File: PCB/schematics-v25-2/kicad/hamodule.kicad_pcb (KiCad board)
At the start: 4 copper layers, 129.6 x 83.3 mm, 200 parts, among them J1 GND|5V, J10 Tx|Rx, J11 Sda|Scl, J12 3|9, J13 13|12, J14 3.3v|GND|7|15, J15 2604-1104, J16 2604-1104, J17 TestPoint, J19 TestPoint, J2 2604-1102, J3 USB_C_Receptacle_USB2.0, J4 GND|3.3V, J5 Conn_01x02_Pin, J6 2604-1104, J7 2604-1104, J8 5v|GND|Do, J9 Screen, K1 AQG22205, K2 AQG22205, K3 AQG22205, K4 AQG22205, K5 AQG22205, K6 AQG22205, K7 AQG22205, K8 AQG22205, SW1 USB | PS, SW2 Reset, SW3 Boot, U1 LD1117AV33, U10 SN74LV1T34DBV, U11 ULN2803A, U12 TCAL6416, U14 74AHC1G04, U2 USBLC6-2SC6, U3 ESP32-S3-WROOM-2, U4 LDA210, U5 LDA210, U6 LDA210, U7 LDA210, U8 SHT4x, U9 SN74LVCH8T245

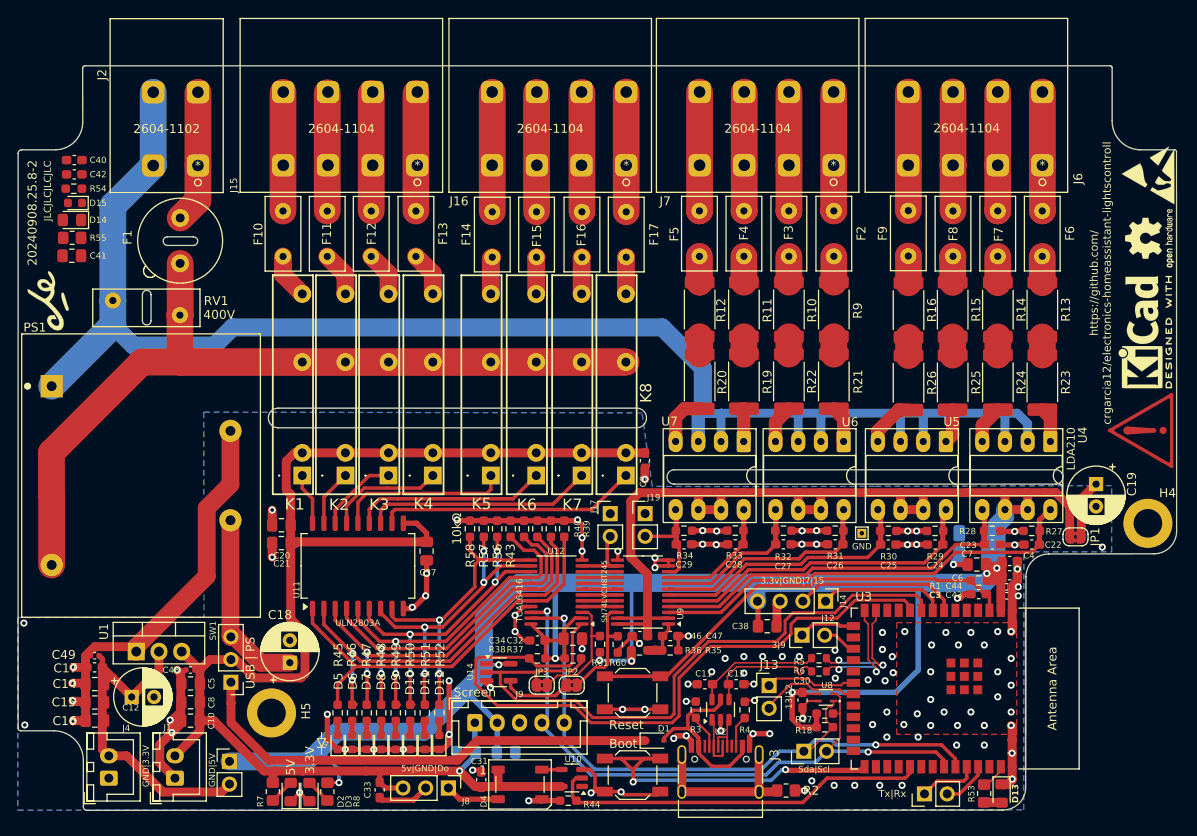
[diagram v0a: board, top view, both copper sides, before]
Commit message: Adding GND vias close to signal. Separate signal vias to make sure that they dont create a large cut in layer 2 and 3. For example for the LEDs going to ULN or the R56, R57, etc. Their vias are not aligned anymore allowing copper between them in layers 2 and 3. Check the videos from Rick Hartley - How to achieve proper grounding and from Hans Rosenberg: Flawless PCB design Part 2
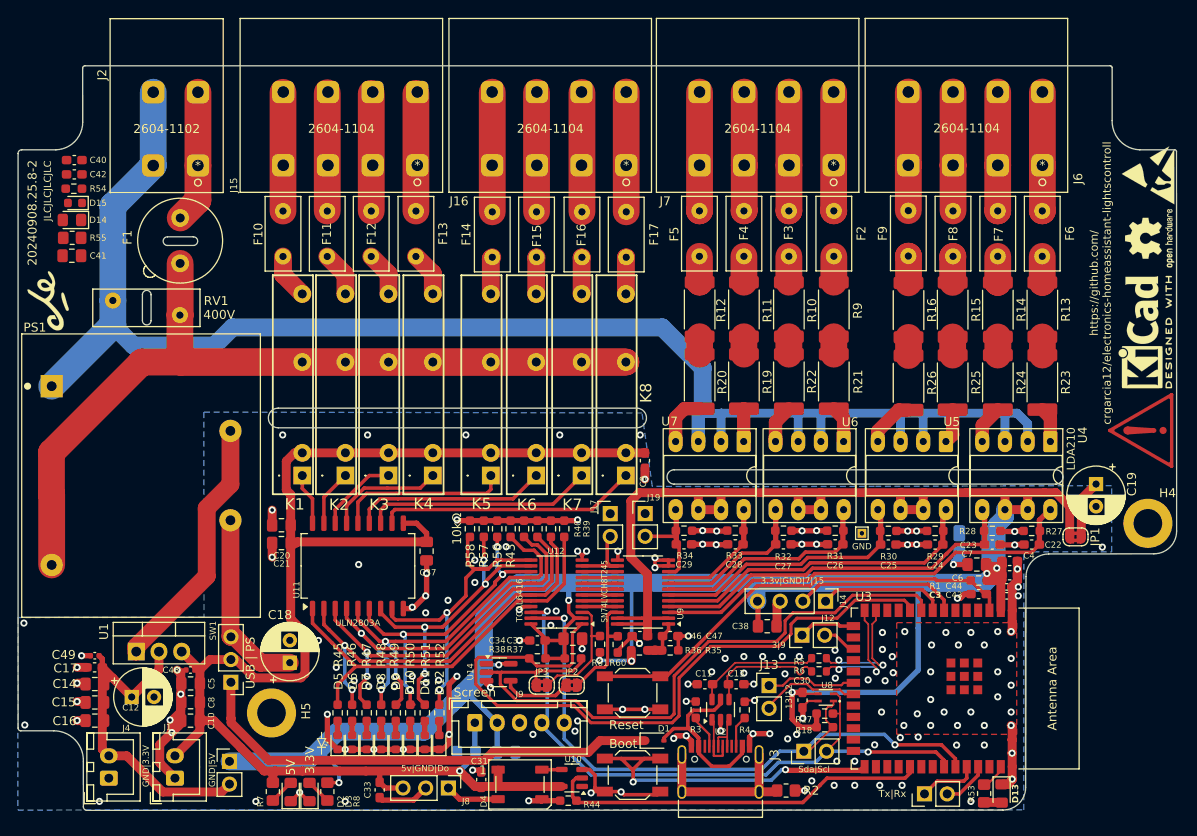
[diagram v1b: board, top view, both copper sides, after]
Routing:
- net 3.3V+: track 353.4 -> 331.2 mm
- net GND: track 248.3 -> 228.5 mm, vias 123 -> 159
- net Net-(U11-I4): track 40.2 -> 43.4 mm
- net Net-(U11-I8): track 34.5 -> 36.9 mm
- net Net-(U11-I2): track 44.1 -> 45.3 mm
- net Net-(U11-I5): track 38.8 -> 39.9 mm
- net Net-(U11-I7): track 34.7 -> 35.6 mm
- net Net-(U11-I3): track 41.7 -> 42.4 mm
- net SDA: track 73.7 -> 74.2 mm

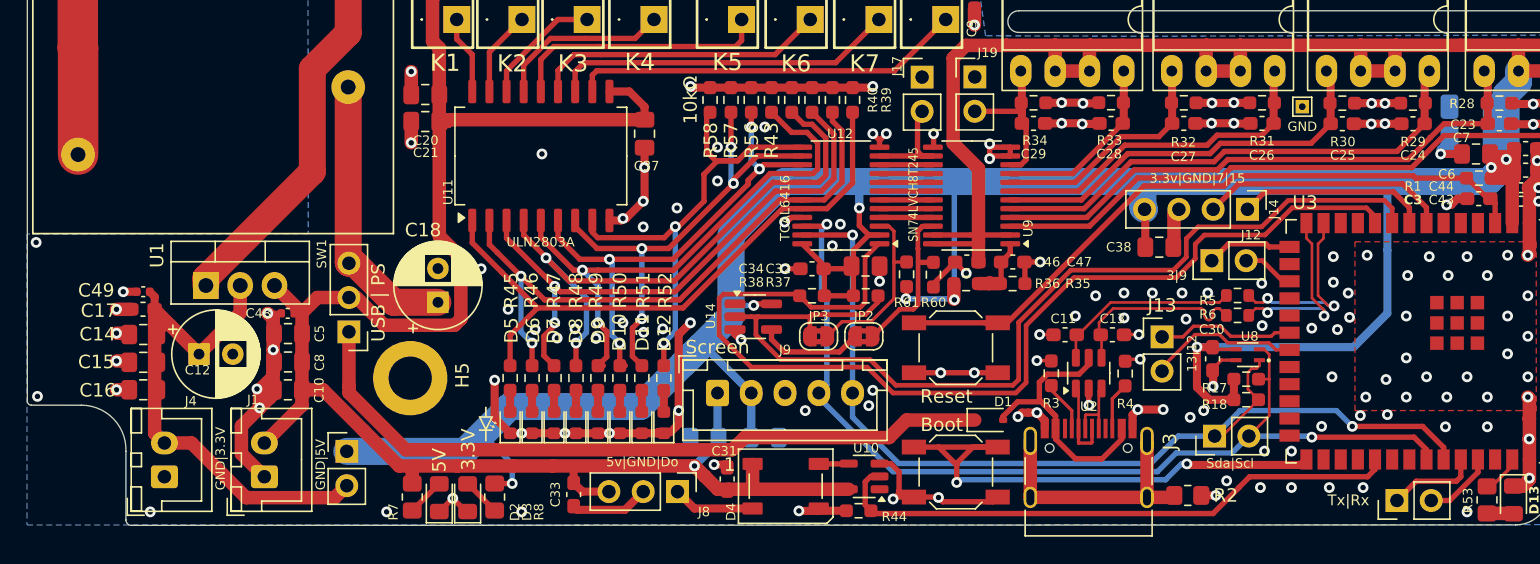
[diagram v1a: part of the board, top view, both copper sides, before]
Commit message: Changes in the schematic look: 1. Align label text to the right, in order the trace is under the label. 2. Display resistors values for the resistors next to the LED (R45... R5x) 3. Align the identifier text for USB protection diodes
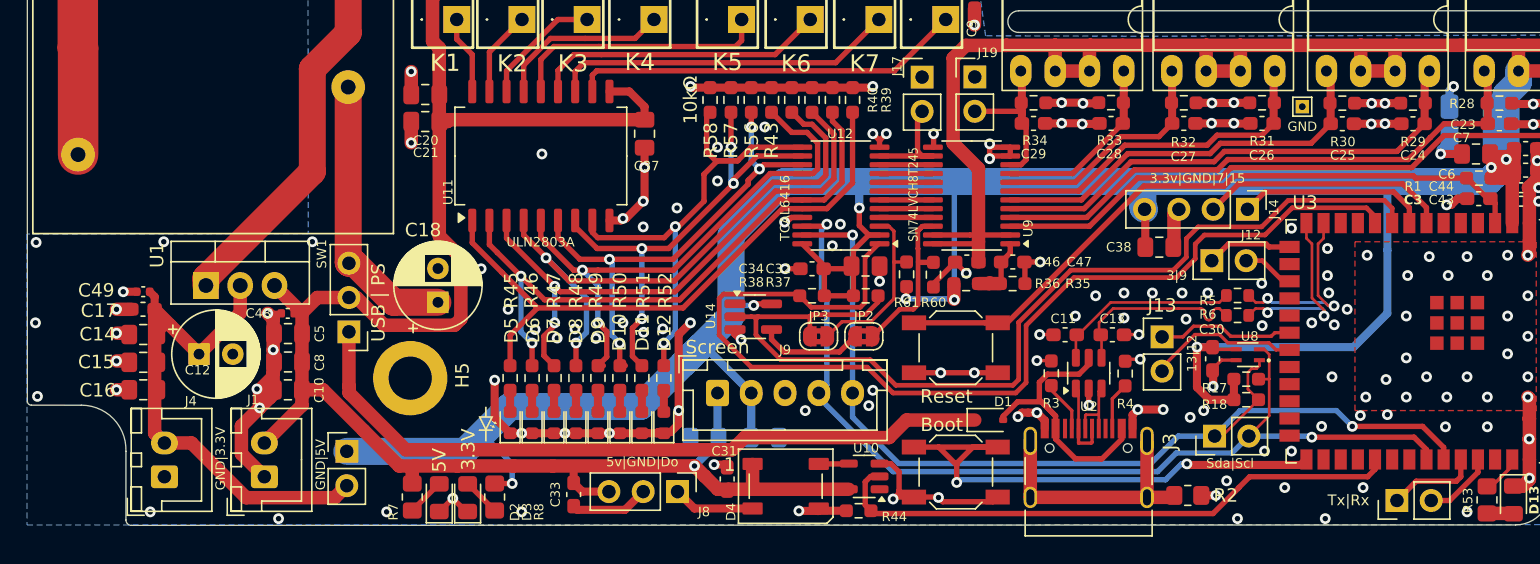
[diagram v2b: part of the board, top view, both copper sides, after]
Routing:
- net GND: track 228.5 -> 230.1 mm, vias 159 -> 165
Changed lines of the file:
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@@
 	)
 	(via
-		(at 120.6 95.6)
+		(at 120.165402 95)
 		(size 0.8)
 		(drill 0.4)
@@
 	)
 	(via
-		(at 120.6 97.5)
+		(at 120.165402 97)
 		(size 0.8)
 		(drill 0.4)
@@
 	)
 	(via
-		(at 121.8 100.1)
+		(at 121.623872 99.502349)
 		(size 0.8)
 		(drill 0.4)
@@
 	)
 	(via
-		(at 117.5 112.7)
+		(at 117 112.7)
 		(size 0.8)
 		(drill 0.4)
@@
 	)
 	(via
+		(at 34 94.5)
+		(size 0.8)
+		(drill 0.4)
+		(layers "F.Cu" "B.Cu")
+		(free yes)
+		(net 16)
+	)
+	(via
 		(at 68 100.5)
 		(size 0.8)
@@
 	)
 	(via
-		(at 119 100.9)
+		(at 45 94.5)
+		(size 0.8)
+		(drill 0.4)
+		(layers "F.Cu" "B.Cu")
+		(free yes)
+		(net 16)
+	)
+	(via
+		(at 119 100.5)
 		(size 0.8)
 		(drill 0.4)
@@
 	)
 	(via
-		(at 120.3 112.7)
+		(at 117.5 93.5)
+		(size 0.8)
+		(drill 0.4)
+		(layers "F.Cu" "B.Cu")
+		(free yes)
+		(net 16)
+	)
+	(via
+		(at 120 115)
 		(size 0.8)
 		(drill 0.4)
@@
 	)
 	(via
+		(at 24.5 100.5)
+		(size 0.8)
+		(drill 0.4)
+		(layers "F.Cu" "B.Cu")
+		(free yes)
+		(net 16)
+	)
+	(via
 		(at 113.2332 85.725)
 		(size 0.8)
@@
 	)
 	(via
-		(at 121.7 98.3)
+		(at 120.258346 98.284493)
 		(size 0.8)
 		(drill 0.4)
@@
 	)
 	(via
+		(at 129.5 83)
+		(size 0.8)
+		(drill 0.4)
+		(layers "F.Cu" "B.Cu")
+		(free yes)
+		(net 16)
+	)
+	(via
 		(at 126 103.1)
 		(size 0.8)
@@
 	)
 	(via
+		(at 42.5 115)
+		(size 0.8)
+		(drill 0.4)
+		(layers "F.Cu" "B.Cu")
+		(free yes)
+		(net 16)
+	)
+	(via
 		(at 113.2332 84.201)
 		(size 0.8)
@@
 	)
 	(via
-		(at 115.2 112.7)
-		(size 0.8)
-		(drill 0.4)
-		(layers "F.Cu" "B.Cu")
-		(free yes)
-		(net 16)
-	)
-	(via
-		(at 120.9 101)
+		(at 113.5 115)
+		(size 0.8)
+		(drill 0.4)
+		(layers "F.Cu" "B.Cu")
+		(free yes)
+		(net 16)
+	)
+	(via
+		(at 120.669 100.646856)
 		(size 0.8)
 		(drill 0.4)
@@
 		(drill 0.4)
 		(layers "F.Cu" "B.Cu")
+		(net 16)
+	)
+	(segment
+		(start 129.2 83.3)
+		(end 129.5 83)
+		(width 0.6)
+		(layer "B.Cu")
 		(net 16)
 	)
@@
 		(width 0.6)
 		(layer "B.Cu")
+		(net 16)
+	)
+	(segment
+		(start 129.2 84.5)
+		(end 129.2 83.3)
+		(width 0.6)
+		(layer "B.Cu")

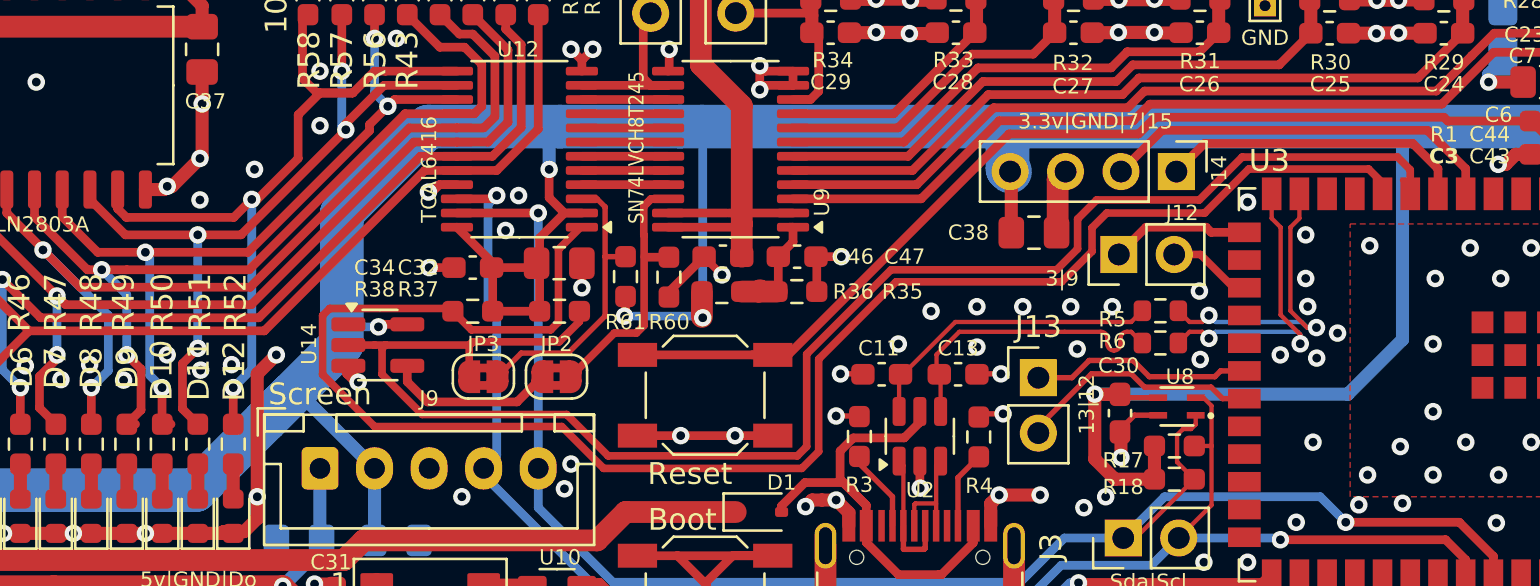
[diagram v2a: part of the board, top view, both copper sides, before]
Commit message: minor changes in vias
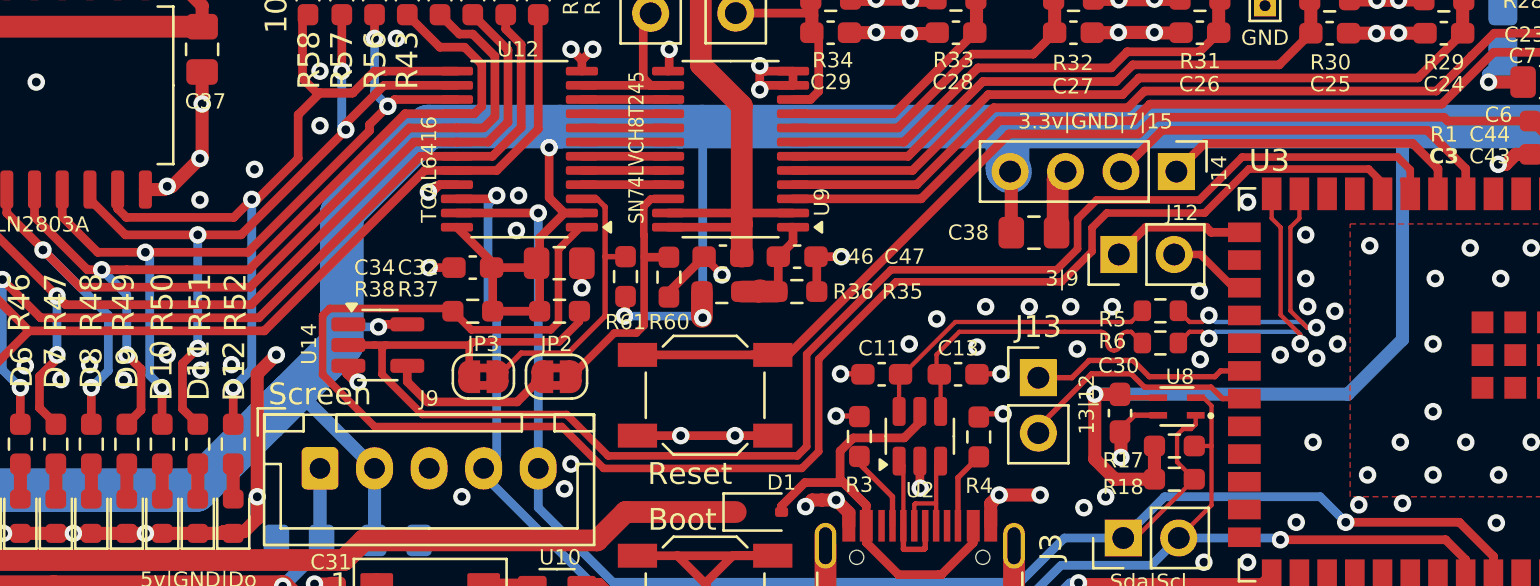
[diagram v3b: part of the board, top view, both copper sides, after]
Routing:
- net GND: vias 165 -> 166
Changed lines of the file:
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@@
 	)
 	(segment
+		(start 85.5 93.298792)
+		(end 86.201208 94)
+		(width 0.4)
+		(layer "F.Cu")
+		(net 3)
+	)
+	(segment
 		(start 84.725 96.5)
 		(end 84.925 96.3)
@@
 	)
 	(segment
-		(start 85.5 92)
-		(end 85.5 93.298792)
-		(width 0.4)
-		(layer "F.Cu")
-		(net 3)
-	)
-	(segment
 		(start 100.0013 79.957418)
 		(end 100 79.956118)
@@
 	)
 	(segment
-		(start 85.5 93.298792)
-		(end 86.201208 94)
-		(width 0.4)
-		(layer "F.Cu")
-		(net 3)
-	)
-	(segment
 		(start 133.975 89.770402)
 		(end 133.845402 89.9)
@@
 	)
 	(segment
+		(start 85.5 91)
+		(end 85.5 93.298792)
+		(width 0.4)
+		(layer "F.Cu")
+		(net 3)
+	)
+	(segment
 		(start 100.0013 81.8596)
 		(end 102.5413 81.8596)
@@
 	)
 	(via
-		(at 85.5 92)
+		(at 85.5 91)
 		(size 0.8)
 		(drill 0.4)
@@
 	)
 	(segment
-		(start 85.5 90.539447)
-		(end 86 90.039447)
-		(width 0.6)
-		(layer "B.Cu")
-		(net 3)
-	)
-	(segment
 		(start 59.8 112.4)
 		(end 59.8 110.9374)
@@
 	)
 	(segment
+		(start 85.5 90.539447)
+		(end 86 90.039447)
+		(width 0.6)
+		(layer "B.Cu")
+		(net 3)
+	)
+	(segment
 		(start 110.5 102.3)
 		(end 122.1 102.3)
@@
 	)
 	(segment
+		(start 85.5 91)
+		(end 85.5 90.539447)
+		(width 0.6)
+		(layer "B.Cu")
+		(net 3)
+	)
+	(segment
 		(start 77.5 105.7)
 		(end 74.05 102.25)
@@
 	)
 	(segment
-		(start 85.5 92)
-		(end 85.5 90.539447)
-		(width 0.6)
-		(layer "B.Cu")
-		(net 3)
-	)
-	(segment
 		(start 76 94)
 		(end 79.960553 90.039447)
@@
 	)
 	(via
-		(at 105.1 98.292198)
+		(at 105.5 98.292198)
 		(size 0.8)
 		(drill 0.4)
@@
 	)
 	(via
-		(at 103 98.5)
+		(at 103.258465 98.851686)
 		(size 0.8)
 		(drill 0.4)
@@
 	)
 	(via
-		(at 121.623872 99.502349)
+		(at 121.623872 100)
 		(size 0.8)
 		(drill 0.4)
@@
 	)
 	(via
-		(at 83.503393 94.8)
+		(at 84 94.8)
 		(size 0.8)
 		(drill 0.4)
@@
 	)
 	(via
+		(at 121.5 98.5)
+		(size 0.8)
+		(drill 0.4)
+		(layers "F.Cu" "B.Cu")
+		(free yes)
+		(net 16)
+	)
+	(via
 		(at 106.2 101.369699)
 		(size 0.8)
@@
 	)
 	(via
-		(at 124.5 104.7)
+		(at 124.5 104.5)
 		(size 0.8)
 		(drill 0.4)
@@
 	)
 	(via
-		(at 107.2 98.292198)
+		(at 107.5 98.292198)
 		(size 0.8)
 		(drill 0.4)
@@
 	)
 	(via
-		(at 101.5 100)
+		(at 102 100)
 		(size 0.8)
 		(drill 0.4)
@@
 	)
 	(segment
-		(start 66.538496 103.664604)
-		(end 66.549896 103.676004)
-		(width 0.4)
-		(layer "F.Cu")
-		(net 166)
-	)
-	(segment
 		(start 82.4135 87.189708)
 		(end 82.4135 89.110292)
@@
 		(width 0.4)
 		(layer "F.Cu")
-		(net 169)
-	)
-	(segment
-		(start 68.124696 103.625204)
-		(end 68.175496 103.676004)
-		(width 0.4)
-		(layer "F.Cu")
